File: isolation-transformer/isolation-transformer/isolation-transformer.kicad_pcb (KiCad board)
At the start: 4 copper layers, 100 x 100 mm, 22 parts, among them J1 Conn_BNC_Vert_PCB, J2 Conn_BNC_Vert_PCB, J3 Conn_BNC_Vert_PCB, J4 Conn_BNC_Vert_PCB, T1 Hammond_560, T2 Hammond_560

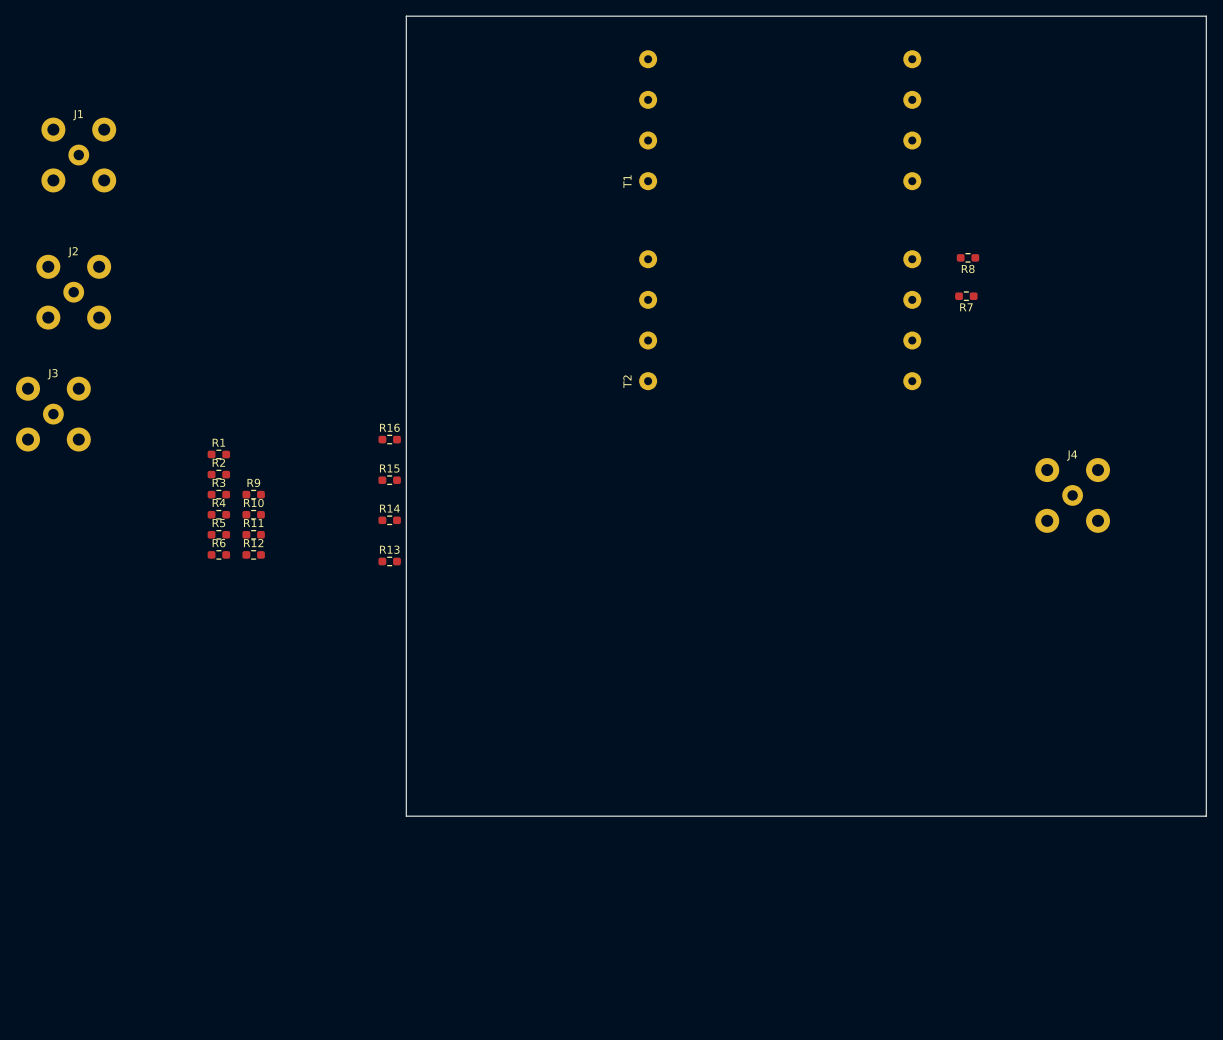
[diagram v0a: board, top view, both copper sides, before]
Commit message: fix: add shield pin connect options
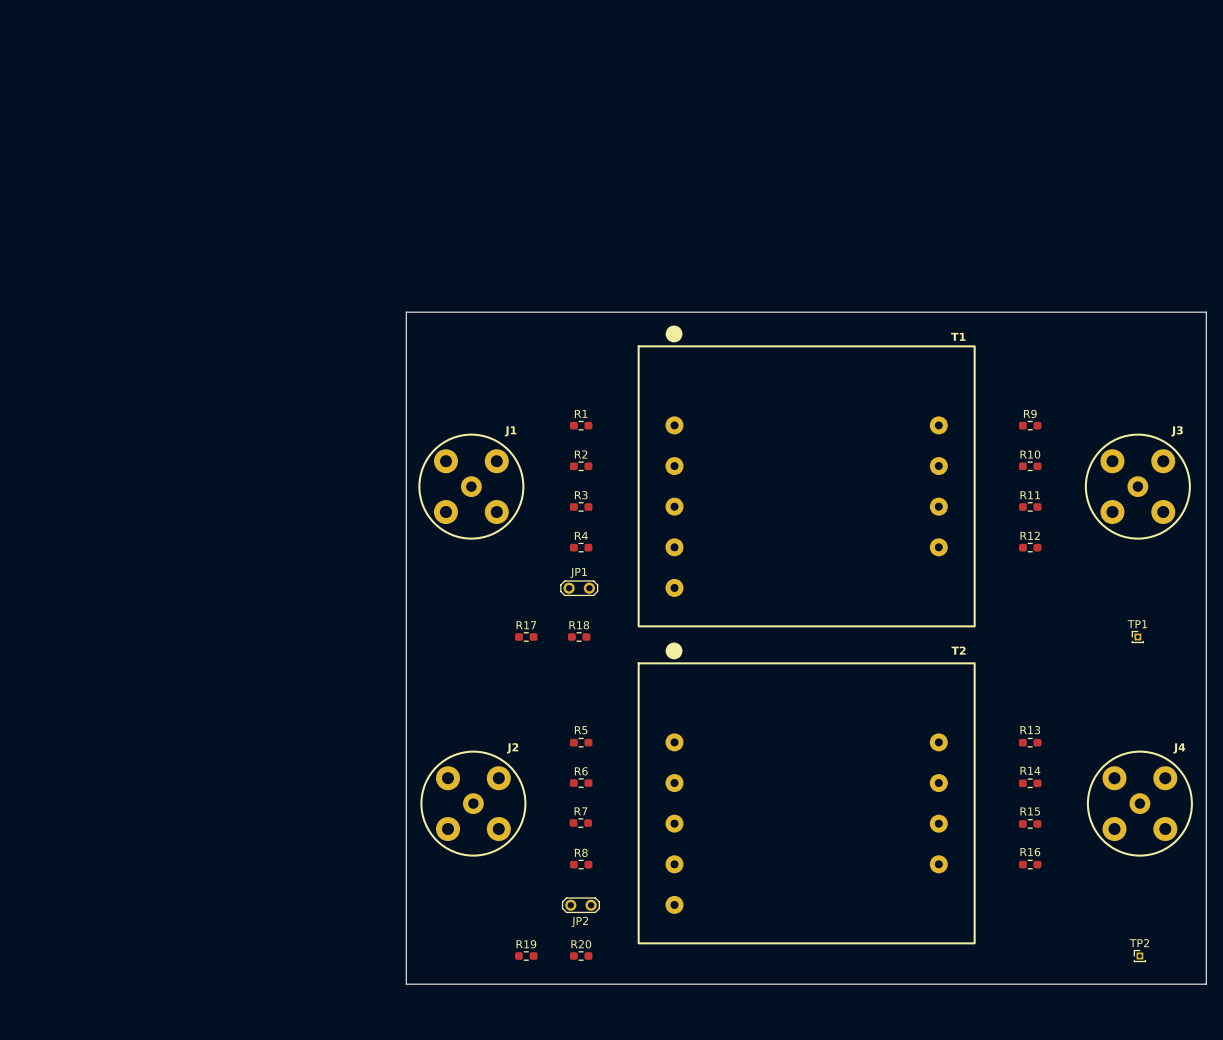
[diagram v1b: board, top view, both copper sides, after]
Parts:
- added JP1: Jumper_2_Bridged, TestPoint:TestPoint_2Pads_Pitch2.54mm_Drill0.8mm, F.Cu at (120.3, 100.5)
- added JP2: Jumper_2_Bridged, TestPoint:TestPoint_2Pads_Pitch2.54mm_Drill0.8mm, F.Cu at (123.1, 140.1)
- added R17: 0, Resistor_SMD:R_0603_1608Metric_Pad0.98x0.95mm_HandSolder, F.Cu at (115.0, 106.6)
- added R18: 0, Resistor_SMD:R_0603_1608Metric_Pad0.98x0.95mm_HandSolder, F.Cu at (121.6, 106.6)
- added R19: 0, Resistor_SMD:R_0603_1608Metric_Pad0.98x0.95mm_HandSolder, F.Cu at (115.0, 146.5)
- added R20: 0, Resistor_SMD:R_0603_1608Metric_Pad0.98x0.95mm_HandSolder, F.Cu at (121.8, 146.5)
- added TP1: TestPoint, Connector_PinHeader_1.00mm:PinHeader_1x01_P1.00mm_Vertical, F.Cu at (191.4, 106.6)
- added TP2: TestPoint, Connector_PinHeader_1.00mm:PinHeader_1x01_P1.00mm_Vertical, F.Cu at (191.7, 146.5)
- moved J3 135.9 mm to (191.4, 87.8)
- moved R9 97.4 mm to (178.0, 80.2)
- moved R10 97.3 mm to (178.0, 85.3)
- moved R11 97.1 mm to (178.0, 90.3)
- moved R12 97.1 mm to (178.0, 95.4)
- moved R16 96.1 mm to (178.0, 135.0), turned to 180 degrees
- moved R15 90.9 mm to (178.0, 130.0), turned to 180 degrees
- moved R8 89.9 mm to (121.8, 135.0), turned to 0 degrees
- moved R14 86.5 mm to (178.0, 124.9), turned to 180 degrees
- moved R13 83.2 mm to (178.0, 119.8), turned to 180 degrees
- moved R7 81.6 mm to (121.8, 129.9), turned to 0 degrees
- moved J2 81.1 mm to (108.4, 127.4)
- moved J1 64.2 mm to (108.1, 87.8)
- moved T2 60.4 mm to (150.0, 127.4), turned to 0 degrees
- moved R6 53.5 mm to (121.8, 124.9)
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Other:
- board size 100 x 100 mm -> 100 x 84 mm

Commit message: feat: add 3D models and GND jmpr
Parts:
- added H1: MountingHole_Pad, MountingHole:MountingHole_3.2mm_M3_Pad, F.Cu at (104.8, 70.8)
- added H2: MountingHole_Pad, MountingHole:MountingHole_3.2mm_M3_Pad, F.Cu at (104.8, 145.2)
- added H3: MountingHole_Pad, MountingHole:MountingHole_3.2mm_M3_Pad, F.Cu at (195.2, 145.2)
- added H4: MountingHole_Pad, MountingHole:MountingHole_3.2mm_M3_Pad, F.Cu at (195.2, 70.8)
- added JP3: Jumper_2_Bridged, TestPoint:TestPoint_2Pads_Pitch2.54mm_Drill0.8mm, F.Cu at (122.8, 103.3)
- added JP4: Jumper_2_Bridged, TestPoint:TestPoint_2Pads_Pitch2.54mm_Drill0.8mm, F.Cu at (123.1, 142.9)
- moved TP2 6.38 mm to (191.7, 140.1)
- moved TP1 6.13 mm to (191.4, 100.5)
- moved JP2 2.52 mm to (120.6, 140.1), turned to 0 degrees
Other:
- rule pad_to_mask_clearance: 0 -> 0.051
- board text added: "0"
- board text added: "0 mm"
- board text added: "0.0000 mm / 0.0000 mm"
- board text added: "0.01 mm"
- board text added: "0.02"
- board text added: "0.035 mm"
- board text added: "0.1 mm"
- board text added: "0.3000 mm"
- board text added: "1"
- board text added: "1.24 mm"
- board text added: "1.6000 mm"
- board text added: "100.0000 mm x 84.0000 mm"
- board text added: "3.3"
- board text added: "4"
- board text added: "4.4"
- board text added: "B.Cu"
- board text added: "B.Mask"
- board text added: "B.Paste"
- board text added: "B.Silkscreen"
- board text added: "BOARD CHARACTERISTICS"
- board text added: "Black"
- board text added: "Board Thickness:"
- board text added: "Board overall dimensions:"
- board text added: "Bottom Silk Screen"
- board text added: "Bottom Solder Mask"
- board text added: "Bottom Solder Paste"
- board text added: "Castellated pads:"
- board text added: "Color"
- board text added: "Copper Finish:"
- board text added: "Copper Layer Count:"
- board text added: "Dielectric"
- board text added: "Edge card connectors:"
- board text added: "Epsilon R"
- board text added: "F.Cu"
- board text added: "F.Mask"
- board text added: "F.Paste"
- board text added: "F.Silkscreen"
- board text added: "FR4"
- board text added: "FR4 natural"
- board text added: "HAL SnPb"
- board text added: "Impedance Control:"
- board text added: "In1.Cu"
- board text added: "In2.Cu"
- board text added: "Layer Name"
- board text added: "Loss Tangent"
- board text added: "Material"
- board text added: "Min hole diameter:"
- board text added: "Min track/spacing:"
- board text added: "No"
- board text added: "Not specified"
- board text added: "Plated Board Edge:"
- board text added: "Thickness (mm)"
- board text added: "Top Silk Screen"
- board text added: "Top Solder Mask"
- board text added: "Top Solder Paste"
- board text added: "Type"
- board text added: "White"
- board text added: "copper"
- board text added: "core"
- board text added: "prepreg"

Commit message: feat: input signal routing
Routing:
- net Net-(R18-Pad2): track 0.00 -> 71.5 mm
- net Net-(J2-Ext): track 0.00 -> 59.5 mm, vias 0 -> 2
- net Net-(J1-Ext): track 0.00 -> 59.2 mm, vias 0 -> 2
- net Net-(J3-Ext): track 0.00 -> 25.4 mm
- net Net-(J4-Ext): track 0.00 -> 25.4 mm
- net Net-(J1-In): track 0.00 -> 22.8 mm, vias 0 -> 2
- net Net-(J2-In): track 0.00 -> 22.4 mm, vias 0 -> 2
- net Net-(T2-IN1A): track 0.00 -> 11.0 mm
- net Net-(T2-IN2A): track 0.00 -> 10.8 mm
- net Net-(T1-IN2A): track 0.00 -> 10.8 mm
- net Net-(R8-Pad2): track 0.00 -> 10.8 mm
- net Net-(R4-Pad2): track 0.00 -> 10.8 mm
- net Net-(T1-IN1B): track 0.00 -> 10.8 mm
- net Net-(T1-IN1A): track 0.00 -> 10.8 mm
- net Net-(T2-IN1B): track 0.00 -> 10.8 mm
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
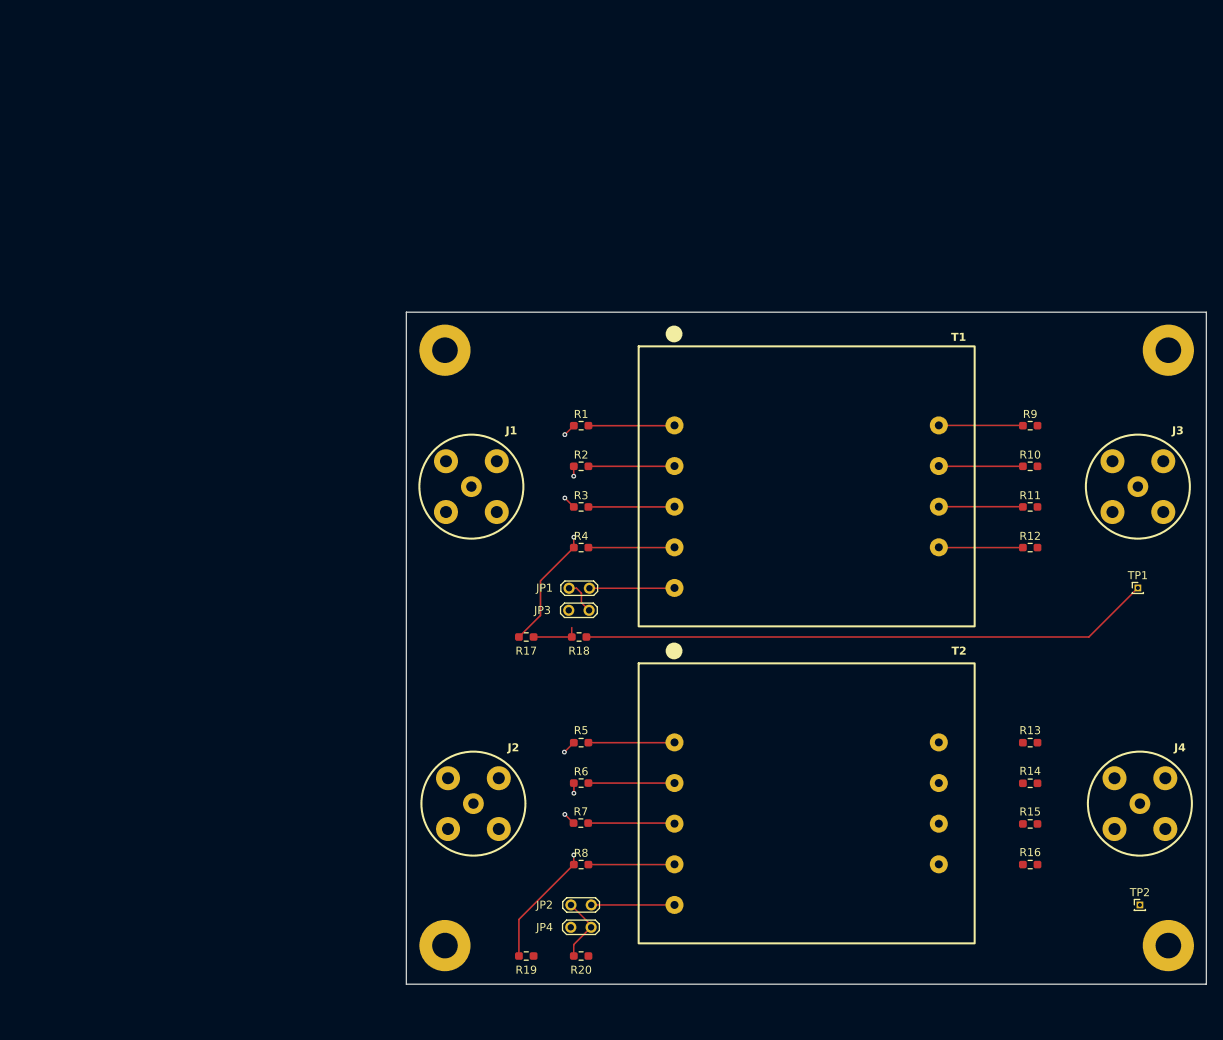
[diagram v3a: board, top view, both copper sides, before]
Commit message: feat: secondary side routing and GND zones
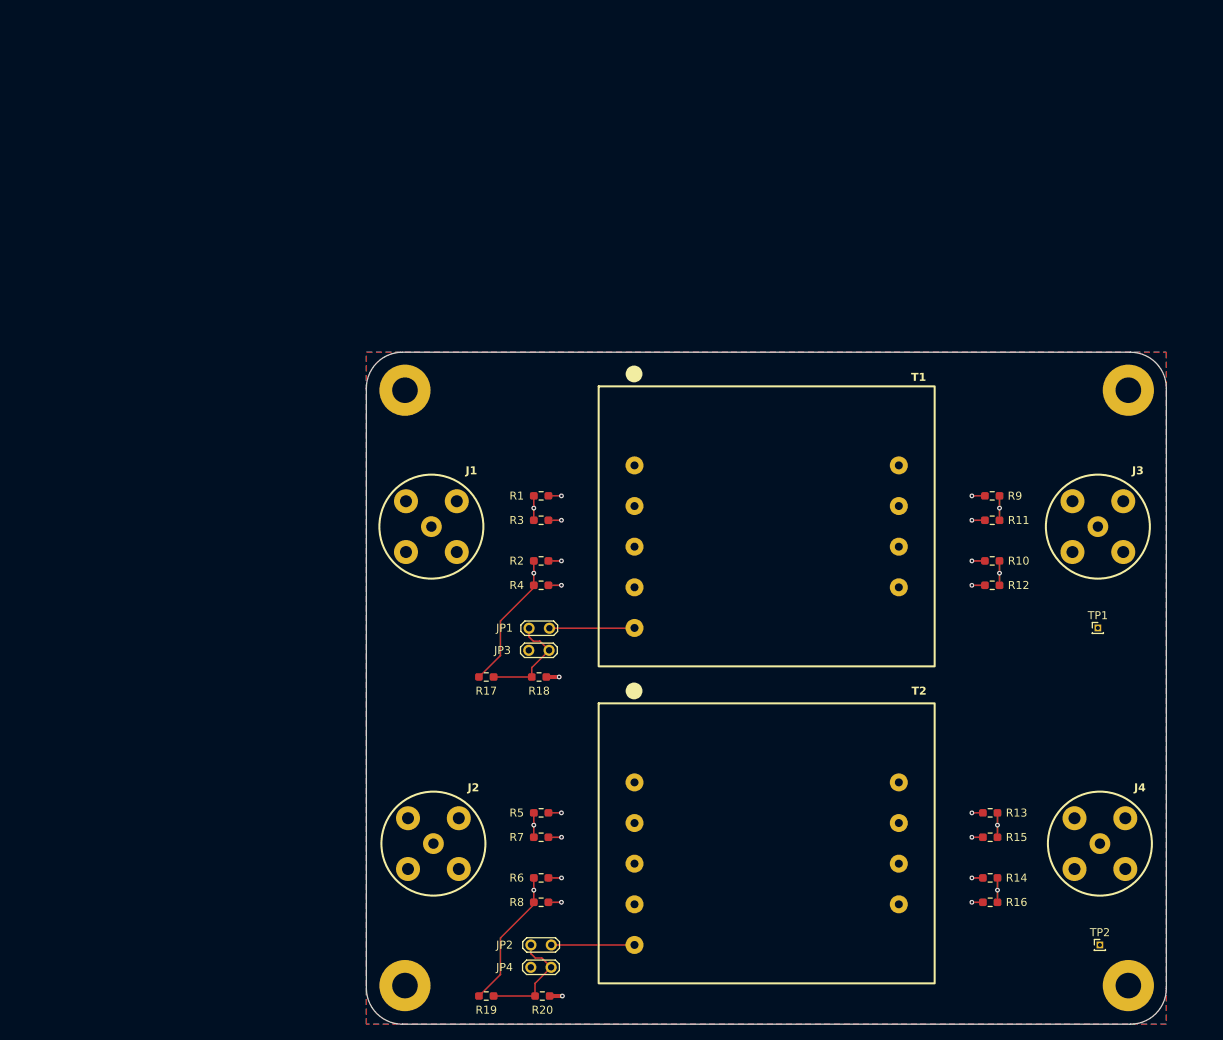
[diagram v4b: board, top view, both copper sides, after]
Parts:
- moved R6 12.9 mm to (116.8, 136.7)
- moved R2 12.8 mm to (116.8, 97.1)
- moved R14 12.8 mm to (173.0, 136.7), turned to 0 degrees
- moved R10 12.7 mm to (173.2, 97.1)
- moved R1 10.1 mm to (116.8, 89.0)
- moved R13 10.1 mm to (173.0, 128.6), turned to 0 degrees
- moved R5 10.1 mm to (116.8, 128.6)
- moved R9 9.98 mm to (173.2, 89.0)
- moved J2 7.07 mm to (103.4, 132.4)
- moved J4 7.07 mm to (186.7, 132.4)
- moved H1 7.07 mm to (99.8, 75.8)
- moved H2 7.07 mm to (99.8, 150.2)
- moved H3 7.07 mm to (190.2, 150.2)
- moved H4 7.07 mm to (190.2, 75.8)
- moved J1 7.07 mm to (103.1, 92.8)
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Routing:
- net Net-(R20-Pad2): track 0.00 -> 71.4 mm, vias 0 -> 1
- net Net-(J4-In): track 0.00 -> 16.8 mm, vias 0 -> 1
- net Net-(J3-In): track 0.00 -> 16.3 mm, vias 0 -> 1
- net Net-(J4-Ext): track 25.4 -> 39.2 mm, vias 0 -> 1
- net Net-(T2-OUT1B): track 0.00 -> 13.3 mm, vias 0 -> 1
- net Net-(J3-Ext): track 25.4 -> 38.7 mm, vias 0 -> 1
- net Net-(T2-OUT1A): track 0.00 -> 12.1 mm, vias 0 -> 1
- net Net-(T2-OUT2A): track 0.00 -> 11.9 mm, vias 0 -> 1
- net Net-(T2-OUT2B): track 0.00 -> 10.6 mm, vias 0 -> 1
- net Net-(J2-Ext): track 59.5 -> 53.5 mm, vias 2 -> 1
- net Net-(J1-In): track 22.8 -> 16.8 mm, vias 2 -> 1
- net Net-(J2-In): track 22.4 -> 16.6 mm, vias 2 -> 1
- net Net-(J1-Ext): track 59.2 -> 53.5 mm, vias 2 -> 1
- net Net-(JP2-A): track 8.32 -> 13.9 mm
- net Net-(T1-OUT1B): track 10.5 -> 13.6 mm, vias 0 -> 1
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- added copper zone on B.Cu, net GND
- added copper zone on F.Cu, net GND
- added copper zone on In1.Cu, net GND
- added copper zone on In2.Cu, net GND
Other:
- outline, holes or cut-outs redrawn
